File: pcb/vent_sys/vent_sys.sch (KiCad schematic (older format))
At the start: 19 parts, among them J1 Conn_01x02_Female, J2 Conn_01x02_Female, Q1 BT138-600, U1 PC817, U2 stm32f103c8t6-module-china, U3 MOC3021M, U4 RA-02

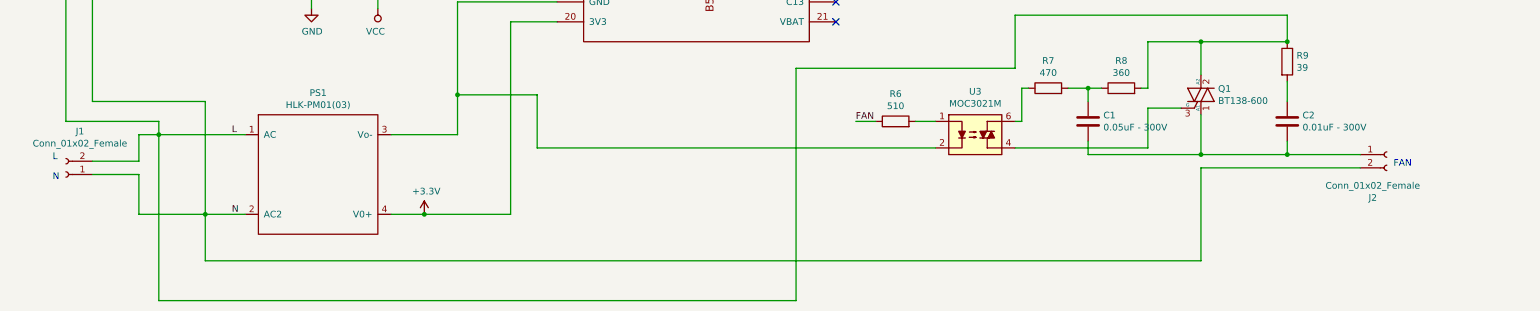
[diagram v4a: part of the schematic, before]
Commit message: add net list and foot prints
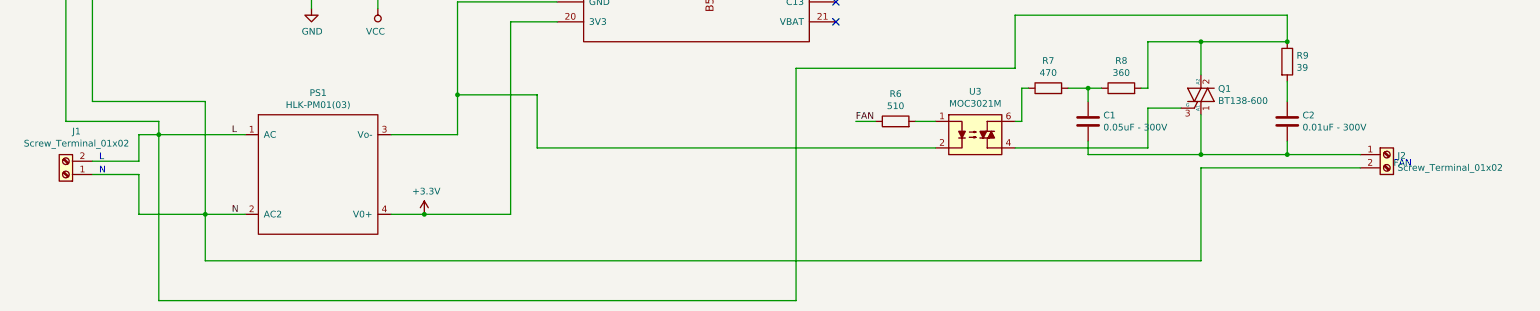
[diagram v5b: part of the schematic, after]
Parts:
- removed J1, J2: Conn_01x02_Female, symbol Connector:Conn_01x02_Female
- added J1, J2: Screw_Terminal_01x02, Connector_Phoenix_MC_HighVoltage:PhoenixContact_MCV_1,5_2-G-5.08_1x02_P5.08mm_Vertical, symbol Connector:Screw_Terminal_01x02
- C1: footprint (none) -> Capacitor_THT:C_Rect_L10.0mm_W2.5mm_P7.50mm_MKS4
- C2: footprint (none) -> Capacitor_THT:C_Rect_L9.0mm_W9.8mm_P7.50mm_MKT
- R6: footprint (none) -> Resistor_SMD:R_0805_2012Metric_Pad1.15x1.40mm_HandSolder
- R7, R8, R9: footprint (none) -> Resistor_THT:R_Axial_DIN0207_L6.3mm_D2.5mm_P10.16mm_Horizontal
- U2: footprint (none) -> Module:Maple_Mini
- U3: footprint (none) -> Package_DIP:DIP-6_W10.16mm
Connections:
- net L: now also J1.2 (Pin_2)
- net N: now also J1.1 (Pin_1), J2.2 (Pin_2)
- net at C1.2, C2.2, Q1.1 (A1): now also J2.1 (Pin_1)
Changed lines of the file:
@@
 F 0 "U2" H 5700 4837 60  0000 C CNN
 F 1 "stm32f103c8t6-module-china" H 5700 4731 60  0000 C CNN
-F 2 "" H 5700 1400 60  0001 C CNN
+F 2 "Module:Maple_Mini" H 5700 1400 60  0001 C CNN
 F 3 "" H 5300 3350 60  0000 C CNN
 	1    5700 3100
@@
 $EndComp
 $Comp
-L power:+3.3V #PWR04
+L power:+3.3V #PWR05
 U 1 1 5C5AFAD4
 P 3650 6000
-F 0 "#PWR04" H 3650 5850 50  0001 C CNN
+F 0 "#PWR05" H 3650 5850 50  0001 C CNN
 F 1 "+3.3V" H 3665 6173 50  0000 C CNN
 F 2 "" H 3650 6000 50  0001 C CNN
@@
 Wire Wire Line
 	3400 6000 3650 6000
-$Comp
-L Connector:Conn_01x02_Female J1
-U 1 1 5C5B0053
-P 950 5700
-F 0 "J1" H 844 5375 50  0000 C CNN
-F 1 "Conn_01x02_Female" H 844 5466 50  0000 C CNN
-F 2 "" H 950 5700 50  0001 C CNN
-F 3 "~" H 950 5700 50  0001 C CNN
-	1    950  5700
-	-1   0    0    1
-$EndComp
 $Comp
 L Device:R R3
@@
 Connection ~ 3650 6000
 $Comp
-L power:GND #PWR05
+L power:GND #PWR06
 U 1 1 5C5B0D6D
 P 7250 1500
-F 0 "#PWR05" H 7250 1250 50  0001 C CNN
+F 0 "#PWR06" H 7250 1250 50  0001 C CNN
 F 1 "GND" H 7255 1327 50  0000 C CNN
 F 2 "" H 7250 1500 50  0001 C CNN
@@
 	2800 2650 2800 2500
 $Comp
-L power:+3.3V #PWR06
+L power:+3.3V #PWR07
 U 1 1 5C5B5B03
 P 7500 1800
-F 0 "#PWR06" H 7500 1650 50  0001 C CNN
+F 0 "#PWR07" H 7500 1650 50  0001 C CNN
 F 1 "+3.3V" H 7515 1973 50  0000 C CNN
 F 2 "" H 7500 1800 50  0001 C CNN
@@
 	1650 5400 2300 5400
 $Comp
-L power:GND #PWR07
+L power:GND #PWR08
 U 1 1 5C5D7125
 P 7750 850
-F 0 "#PWR07" H 7750 600 50  0001 C CNN
+F 0 "#PWR08" H 7750 600 50  0001 C CNN
 F 1 "GND" H 7755 677 50  0000 C CNN
 F 2 "" H 7750 850 50  0001 C CNN
@@
 Connection ~ 8400 900
 $Comp
-L power:+3.3V #PWR08
+L power:+3.3V #PWR09
 U 1 1 5C5DA605
 P 8000 1100
-F 0 "#PWR08" H 8000 950 50  0001 C CNN
+F 0 "#PWR09" H 8000 950 50  0001 C CNN
 F 1 "+3.3V" H 8015 1273 50  0000 C CNN
 F 2 "" H 8000 1100 50  0001 C CNN
@@
 Wire Wire Line
 	8000 1100 8500 1100
-Text Notes 850  5600 0    50   ~ 0
+Text Notes 1200 5600 0    50   ~ 0
 L
-Text Notes 850  5750 0    50   ~ 0
+Text Notes 1200 5700 0    50   ~ 0
 N
 Wire Wire Line
@@
 	8700 2900 8700 2200
 $Comp
-L power:PWR_FLAG #FLG02
+L power:PWR_FLAG #FLG01
 U 1 1 5C8AB50F
 P 2800 4350
-F 0 "#FLG02" H 2800 4425 50  0001 C CNN
+F 0 "#FLG01" H 2800 4425 50  0001 C CNN
 F 1 "PWR_FLAG" H 2800 4524 50  0000 C CNN
 F 2 "" H 2800 4350 50  0001 C CNN
@@
 $EndComp
 $Comp
-L power:PWR_FLAG #FLG01
+L power:PWR_FLAG #FLG02
 U 1 1 5C8AB681
 P 3300 4350
-F 0 "#FLG01" H 3300 4425 50  0001 C CNN
+F 0 "#FLG02" H 3300 4425 50  0001 C CNN
 F 1 "PWR_FLAG" H 3300 4524 50  0000 C CNN
 F 2 "" H 3300 4350 50  0001 C CNN
@@
 SCK
 $Comp
-L power:GND #PWR09
+L power:GND #PWR010
 U 1 1 5C8D193A
 P 9600 1700
-F 0 "#PWR09" H 9600 1450 50  0001 C CNN
+F 0 "#PWR010" H 9600 1450 50  0001 C CNN
 F 1 "GND" H 9605 1527 50  0000 C CNN
 F 2 "" H 9600 1700 50  0001 C CNN
@@
 	9600 1600 9600 1700
 $Comp
-L power:GND #PWR010
+L power:GND #PWR011
 U 1 1 5C8D5889
 P 9750 700
-F 0 "#PWR010" H 9750 450 50  0001 C CNN
+F 0 "#PWR011" H 9750 450 50  0001 C CNN
 F 1 "GND" H 9755 527 50  0000 C CNN
 F 2 "" H 9750 700 50  0001 C CNN
@@
 F 0 "C2" H 10265 5346 50  0000 L CNN
 F 1 "0.01uF - 300V" H 10265 5255 50  0000 L CNN
-F 2 "" H 10188 5150 50  0001 C CNN
+F 2 "Capacitor_THT:C_Rect_L9.0mm_W9.8mm_P7.50mm_MKT" H 10188 5150 50  0001 C CNN
 F 3 "~" H 10150 5300 50  0001 C CNN
 	1    10150 5300
@@
 F 0 "R9" H 10220 4896 50  0000 L CNN
 F 1 "39" H 10220 4805 50  0000 L CNN
-F 2 "" V 10080 4850 50  0001 C CNN
+F 2 "Resistor_THT:R_Axial_DIN0207_L6.3mm_D2.5mm_P10.16mm_Horizontal" V 10080 4850 50  0001 C CNN
 F 3 "~" H 10150 4850 50  0001 C CNN
 	1    10150 4850
@@
 F 0 "R7" V 8557 5050 50  0000 C CNN
 F 1 "470" V 8466 5050 50  0000 C CNN
-F 2 "" V 8280 5050 50  0001 C CNN
+F 2 "Resistor_THT:R_Axial_DIN0207_L6.3mm_D2.5mm_P10.16mm_Horizontal" V 8280 5050 50  0001 C CNN
 F 3 "~" H 8350 5050 50  0001 C CNN
 	1    8350 5050
@@
 F 0 "R8" V 9107 5050 50  0000 C CNN
 F 1 "360" V 9016 5050 50  0000 C CNN
-F 2 "" V 8830 5050 50  0001 C CNN
+F 2 "Resistor_THT:R_Axial_DIN0207_L6.3mm_D2.5mm_P10.16mm_Horizontal" V 8830 5050 50  0001 C CNN
 F 3 "~" H 8900 5050 50  0001 C CNN
 	1    8900 5050
@@
 Text Notes 10950 5650 0    50   ~ 0
 FAN
-$Comp
-L Connector:Conn_01x02_Female J2
-U 1 1 5C5DC3CB
-P 10900 5550
-F 0 "J2" H 10794 5225 50  0000 C CNN
-F 1 "Conn_01x02_Female" H 10794 5316 50  0000 C CNN
-F 2 "" H 10900 5550 50  0001 C CNN
-F 3 "~" H 10900 5550 50  0001 C CNN
-	1    10900 5550
-	1    0    0    -1
-$EndComp
 $Comp
 L Device:C C1
@@
 F 0 "C1" H 8765 5346 50  0000 L CNN
 F 1 "0.05uF - 300V" H 8765 5255 50  0000 L CNN
-F 2 "" H 8688 5150 50  0001 C CNN
+F 2 "Capacitor_THT:C_Rect_L10.0mm_W2.5mm_P7.50mm_MKS4" H 8688 5150 50  0001 C CNN
 F 3 "~" H 8650 5300 50  0001 C CNN
 	1    8650 5300
@@
 F 0 "U3" H 7800 5725 50  0000 C CNN
 F 1 "MOC3021M" H 7800 5634 50  0000 C CNN
-F 2 "" H 7600 5200 50  0001 L CIN
+F 2 "Package_DIP:DIP-6_W10.16mm" H 7600 5200 50  0001 L CIN
 F 3 "http://www.fairchildsemi.com/ds/MO/MOC3020M.pdf" H 7775 5400 50  0001 L CNN
 	1    7800 5400
@@
 F 0 "R6" V 7407 5300 50  0000 C CNN
 F 1 "510" V 7316 5300 50  0000 C CNN
-F 2 "" V 7130 5300 50  0001 C CNN
+F 2 "Resistor_SMD:R_0805_2012Metric_Pad1.15x1.40mm_HandSolder" V 7130 5300 50  0001 C CNN
 F 3 "~" H 7200 5300 50  0001 C CNN
 	1    7200 5300
@@
 	3650 6000 4300 6000
 $Comp
-L power:GND #PWR0101
+L power:GND #PWR03
 U 1 1 5C9B68E2
 P 2800 4450
-F 0 "#PWR0101" H 2800 4200 50  0001 C CNN
+F 0 "#PWR03" H 2800 4200 50  0001 C CNN
 F 1 "GND" H 2805 4277 50  0000 C CNN
 F 2 "" H 2800 4450 50  0001 C CNN
@@
 	2800 4350 2800 4450
 $Comp
-L power:VCC #PWR0102
+L power:VCC #PWR04
 U 1 1 5C9BB0DE
 P 3300 4450
-F 0 "#PWR0102" H 3300 4300 50  0001 C CNN
+F 0 "#PWR04" H 3300 4300 50  0001 C CNN
 F 1 "VCC" H 3318 4623 50  0000 C CNN
 F 2 "" H 3300 4450 50  0001 C CNN
@@
 Wire Wire Line
 	2800 3050 3500 3050
+$Comp
+L Connector:Screw_Terminal_01x02 J2
+U 1 1 5C92A326
+P 10900 5550
+F 0 "J2" H 10980 5542 50  0000 L CNN
+F 1 "Screw_Terminal_01x02" H 10980 5451 50  0000 L CNN
+F 2 "Connector_Phoenix_MC_HighVoltage:PhoenixContact_MCV_1,5_2-G-5.08_1x02_P5.08mm_Vertical" H 10900 5550 50  0001 C CNN
+F 3 "~" H 10900 5550 50  0001 C CNN
+	1    10900 5550
+	1    0    0    -1
+$EndComp
+$Comp
+L Connector:Screw_Terminal_01x02 J1
+U 1 1 5C92A382
+P 950 5700
+F 0 "J1" H 870 5375 50  0000 C CNN
+F 1 "Screw_Terminal_01x02" H 870 5466 50  0000 C CNN
+F 2 "Connector_Phoenix_MC_HighVoltage:PhoenixContact_MCV_1,5_2-G-5.08_1x02_P5.08mm_Vertical" H 950 5700 50  0001 C CNN
+F 3 "~" H 950 5700 50  0001 C CNN
+	1    950  5700
+	-1   0    0    1
+$EndComp
 Wire Bus Line
 	10800 750  10800 2100

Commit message: pcb trace
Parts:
- added R10, R11: 5K, Resistor_SMD:R_1206_3216Metric, symbol Device:R
- PS1: footprint HLK-PM01:HLK-PM01 -> Converter_ACDC:HLK-PM01
- U2: symbol stm32f103c8t6-module-china:stm32f103c8t6-module-china -> vent_sys-rescue:stm32f103c8t6-module-china-stm32f103c8t6-module-china
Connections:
- net GND: now also PS1.3 (Vo-), U2.19 (GND), U3.2; no longer U2.39 (GND), U2.40 (GND), U4.1 (gnd), U4.16 (gnd), U4.2 (gnd), U4.9 (gnd)
- net MISO: now also R11.1; no longer U4.13 (miso)
- net MOSI: now also R10.2; no longer U4.14 (mosi)
- net VCC: now also PS1.4 (V0+), U2.20 (3V3)
- net at U2.24 (C15/OSC32_OUT): now also R6.1
- net +3V3: no longer names the net of R5.1, U2.38 (3V3), U4.3 (3v3)
- net +3V3: no longer PS1.4 (V0+), U2.20 (3V3)
- net FAN: no longer names the net of U2.35 (B10/SCL2/U3TX)
- net FAN: no longer R6.1
- new net: U2.39 (GND), U2.40 (GND), U4.1 (gnd), U4.16 (gnd), U4.2 (gnd), U4.9 (gnd)
- new net: R11.2, U4.13 (miso)
- new net: R10.1, U4.14 (mosi)
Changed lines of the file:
@@
 $EndDescr
 $Comp
-L stm32f103c8t6-module-china:stm32f103c8t6-module-china U2
+L vent_sys-rescue:stm32f103c8t6-module-china-stm32f103c8t6-module-china U2
 U 1 1 5C5569F8
 P 5700 3100
@@
 F 0 "PS1" H 2850 6315 50  0000 C CNN
 F 1 "HLK-PM01(03)" H 2850 6224 50  0000 C CNN
-F 2 "HLK-PM01:HLK-PM01" H 2850 5700 50  0001 C CNN
+F 2 "Converter_ACDC:HLK-PM01" H 2850 5700 50  0001 C CNN
 F 3 "" H 2850 5700 50  0001 C CNN
 	1    2850 5700
@@
 	1    0    0    -1
 $EndComp
-$Comp
-L power:+3.3V #PWR05
-U 1 1 5C5AFAD4
-P 3650 6000
-F 0 "#PWR05" H 3650 5850 50  0001 C CNN
-F 1 "+3.3V" H 3665 6173 50  0000 C CNN
-F 2 "" H 3650 6000 50  0001 C CNN
-F 3 "" H 3650 6000 50  0001 C CNN
-	1    3650 6000
-	1    0    0    -1
-$EndComp
-Wire Wire Line
-	3400 6000 3650 6000
 $Comp
 L Device:R R3
@@
 Wire Wire Line
 	4300 4550 4300 6000
-Connection ~ 3650 6000
-$Comp
-L power:GND #PWR06
-U 1 1 5C5B0D6D
-P 7250 1500
-F 0 "#PWR06" H 7250 1250 50  0001 C CNN
-F 1 "GND" H 7255 1327 50  0000 C CNN
-F 2 "" H 7250 1500 50  0001 C CNN
-F 3 "" H 7250 1500 50  0001 C CNN
-	1    7250 1500
-	1    0    0    -1
-$EndComp
-Wire Wire Line
-	6750 1700 6900 1700
-Wire Wire Line
-	6900 1700 6900 1400
-Wire Wire Line
-	6900 1400 7250 1400
-Wire Wire Line
-	7250 1400 7250 1500
-Wire Wire Line
-	6750 1850 6900 1850
-Wire Wire Line
-	6900 1850 6900 1700
-Connection ~ 6900 1700
-Wire Wire Line
-	4650 4400 3900 4400
-Wire Wire Line
-	3900 4400 3900 5100
 Wire Wire Line
 	1800 2900 1800 3050
@@
 Wire Wire Line
 	2800 3050 2800 2950
-$Comp
-L power:+3.3V #PWR02
-U 1 1 5C5B4551
-P 2800 2500
-F 0 "#PWR02" H 2800 2350 50  0001 C CNN
-F 1 "+3.3V" H 2815 2673 50  0000 C CNN
-F 2 "" H 2800 2500 50  0001 C CNN
-F 3 "" H 2800 2500 50  0001 C CNN
-	1    2800 2500
-	1    0    0    -1
-$EndComp
-Wire Wire Line
-	2800 2650 2800 2500
-$Comp
-L power:+3.3V #PWR07
-U 1 1 5C5B5B03
-P 7500 1800
-F 0 "#PWR07" H 7500 1650 50  0001 C CNN
-F 1 "+3.3V" H 7515 1973 50  0000 C CNN
-F 2 "" H 7500 1800 50  0001 C CNN
-F 3 "" H 7500 1800 50  0001 C CNN
-	1    7500 1800
-	1    0    0    -1
-$EndComp
-Wire Wire Line
-	6750 2000 7500 2000
-Wire Wire Line
-	7500 2000 7500 1800
 Wire Wire Line
 	1200 3350 1150 3350
@@
 Wire Wire Line
 	1650 5400 2300 5400
-$Comp
-L power:GND #PWR08
-U 1 1 5C5D7125
-P 7750 850
-F 0 "#PWR08" H 7750 600 50  0001 C CNN
-F 1 "GND" H 7755 677 50  0000 C CNN
-F 2 "" H 7750 850 50  0001 C CNN
-F 3 "" H 7750 850 50  0001 C CNN
-	1    7750 850
-	1    0    0    -1
-$EndComp
 Wire Wire Line
 	8500 900  8400 900
 Wire Wire Line
-	8400 900  8400 750
-Wire Wire Line
-	8400 750  7750 750
-Wire Wire Line
-	7750 750  7750 850
-Wire Wire Line
 	8500 1000 8400 1000
 Wire Wire Line
 	8400 1000 8400 900
-Connection ~ 8400 900
-$Comp
-L power:+3.3V #PWR09
-U 1 1 5C5DA605
-P 8000 1100
-F 0 "#PWR09" H 8000 950 50  0001 C CNN
-F 1 "+3.3V" H 8015 1273 50  0000 C CNN
-F 2 "" H 8000 1100 50  0001 C CNN
-F 3 "" H 8000 1100 50  0001 C CNN
-	1    8000 1100
-	1    0    0    -1
-$EndComp
-Wire Wire Line
-	8000 1100 8500 1100
 Text Notes 1200 5600 0    50   ~ 0
 L
@@
 Wire Wire Line
 	8700 2900 8700 2200
-$Comp
-L power:PWR_FLAG #FLG01
-U 1 1 5C8AB50F
-P 2800 4350
-F 0 "#FLG01" H 2800 4425 50  0001 C CNN
-F 1 "PWR_FLAG" H 2800 4524 50  0000 C CNN
-F 2 "" H 2800 4350 50  0001 C CNN
-F 3 "~" H 2800 4350 50  0001 C CNN
-	1    2800 4350
-	1    0    0    -1
-$EndComp
-$Comp
-L power:PWR_FLAG #FLG02
-U 1 1 5C8AB681
-P 3300 4350
-F 0 "#FLG02" H 3300 4425 50  0001 C CNN
-F 1 "PWR_FLAG" H 3300 4524 50  0000 C CNN
-F 2 "" H 3300 4350 50  0001 C CNN
-F 3 "~" H 3300 4350 50  0001 C CNN
-	1    3300 4350
-	1    0    0    -1
-$EndComp
 Text Label 7300 2900 0    50   ~ 0
 MOSI
@@
 	9500 1000 10700 1000
 Wire Wire Line
-	9500 1100 10700 1100
-Wire Wire Line
-	9500 1200 10700 1200
-Wire Wire Line
 	9500 1300 10700 1300
 Entry Wire Line
@@
 Text Label 9850 1000 0    50   ~ 0
 NSS
-Text Label 9850 1100 0    50   ~ 0
+Text Label 10500 1100 0    50   ~ 0
 MOSI
-Text Label 9850 1200 0    50   ~ 0
+Text Label 10500 1200 0    50   ~ 0
 MISO
 Text Label 9850 1300 0    50   ~ 0
 SCK
-$Comp
-L power:GND #PWR010
-U 1 1 5C8D193A
-P 9600 1700
-F 0 "#PWR010" H 9600 1450 50  0001 C CNN
-F 1 "GND" H 9605 1527 50  0000 C CNN
-F 2 "" H 9600 1700 50  0001 C CNN
-F 3 "" H 9600 1700 50  0001 C CNN
-	1    9600 1700
-	1    0    0    -1
-$EndComp
-Wire Wire Line
-	9500 1600 9600 1600
-Wire Wire Line
-	9600 1600 9600 1700
-$Comp
-L power:GND #PWR011
-U 1 1 5C8D5889
-P 9750 700
-F 0 "#PWR011" H 9750 450 50  0001 C CNN
-F 1 "GND" H 9755 527 50  0000 C CNN
-F 2 "" H 9750 700 50  0001 C CNN
-F 3 "" H 9750 700 50  0001 C CNN
-	1    9750 700
-	1    0    0    -1
-$EndComp
-Wire Wire Line
-	9500 900  9500 600
-Wire Wire Line
-	9500 600  9750 600
-Wire Wire Line
-	9750 600  9750 700
 Wire Wire Line
 	6750 3500 9100 3500
@@
 Wire Wire Line
 	7350 5300 7500 5300
-Text Label 6900 5300 0    50   ~ 0
-FAN
-Text Label 7100 2450 0    50   ~ 0
-FAN
-Wire Wire Line
-	7050 5300 6900 5300
-Wire Wire Line
-	6750 2450 7100 2450
-Wire Wire Line
-	7500 5500 4500 5500
-Wire Wire Line
-	4500 5500 4500 5100
-Wire Wire Line
-	4500 5100 3900 5100
-Connection ~ 3900 5100
-Wire Wire Line
-	3900 5100 3900 5400
 Connection ~ 2800 3050
 Entry Wire Line
@@
 NoConn ~ 6750 4400
 NoConn ~ 6750 4250
-NoConn ~ 6750 4100
 NoConn ~ 6750 3950
 NoConn ~ 4650 1850
@@
 NoConn ~ 6750 2150
 NoConn ~ 10900 3300
-Wire Wire Line
-	3650 6000 4300 6000
-$Comp
-L power:GND #PWR03
-U 1 1 5C9B68E2
-P 2800 4450
-F 0 "#PWR03" H 2800 4200 50  0001 C CNN
-F 1 "GND" H 2805 4277 50  0000 C CNN
-F 2 "" H 2800 4450 50  0001 C CNN
-F 3 "" H 2800 4450 50  0001 C CNN
-	1    2800 4450
-	1    0    0    -1
-$EndComp
-Wire Wire Line
-	2800 4350 2800 4450
-$Comp
-L power:VCC #PWR04
-U 1 1 5C9BB0DE
-P 3300 4450
-F 0 "#PWR04" H 3300 4300 50  0001 C CNN
-F 1 "VCC" H 3318 4623 50  0000 C CNN
-F 2 "" H 3300 4450 50  0001 C CNN
-F 3 "" H 3300 4450 50  0001 C CNN
-	1    3300 4450
-	-1   0    0    1
-$EndComp
-Wire Wire Line
-	3300 4350 3300 4450
 NoConn ~ 9500 1400
 NoConn ~ 9500 1500
 NoConn ~ 8500 1500
 NoConn ~ 8500 1600
-Wire Wire Line
-	3400 5400 3900 5400
 Wire Wire Line
 	4650 1700 3500 1700
@@
 	-1   0    0    1
 $EndComp
+$Comp
+L power:GND #PWR0103
+U 1 1 5C986FC8
+P 7150 5600
+F 0 "#PWR0103" H 7150 5350 50  0001 C CNN
+F 1 "GND" H 7155 5427 50  0000 C CNN
+F 2 "" H 7150 5600 50  0001 C CNN
+F 3 "" H 7150 5600 50  0001 C CNN
+	1    7150 5600
+	1    0    0    -1
+$EndComp
+Wire Wire Line
+	7150 5500 7150 5600
+Wire Wire Line
+	3400 6000 3950 6000
+Wire Wire Line
+	3400 5400 3700 5400
+$Comp
+L power:GND #PWR0101
+U 1 1 5C9AEA36
+P 3700 5500
+F 0 "#PWR0101" H 3700 5250 50  0001 C CNN
+F 1 "GND" H 3705 5327 50  0000 C CNN
+F 2 "" H 3700 5500 50  0001 C CNN
+F 3 "" H 3700 5500 50  0001 C CNN
+	1    3700 5500
+	1    0    0    -1
+$EndComp
+Wire Wire Line
+	3700 5500 3700 5400
+Wire Wire Line
+	7150 5500 7500 5500
+Wire Wire Line
+	9500 900  9500 600
+Connection ~ 8400 900
+Wire Wire Line
+	8400 600  8400 900
+Wire Wire Line
+	9500 600  8400 600
+Wire Wire Line
+	6900 1850 6900 1700
+Wire Wire Line
+	4650 4400 4000 4400
+Wire Wire Line
+	6750 1850 6900 1850
+Wire Wire Line
+	6750 1700 6900 1700
+Connection ~ 6900 1700
+$Comp
+L power:VCC #PWR0107
+U 1 1 5C98C187
+P 3950 5900
+F 0 "#PWR0107" H 3950 5750 50  0001 C CNN
+F 1 "VCC" H 3967 6073 50  0000 C CNN
+F 2 "" H 3950 5900 50  0001 C CNN
+F 3 "" H 3950 5900 50  0001 C CNN
+	1    3950 5900
+	1    0    0    -1
+$EndComp
+Wire Wire Line
+	3950 5900 3950 6000
+Connection ~ 3950 6000
+Wire Wire Line
+	3950 6000 4300 6000
+Wire Wire Line
+	7700 1100 8500 1100
+Wire Wire Line
+	4000 4400 4000 5400
+Wire Wire Line
+	4000 5400 3700 5400
+Connection ~ 3700 5400
+Wire Wire Line
+	6900 600  8400 600
+Wire Wire Line
+	6900 600  6900 1700
+Connection ~ 8400 600
+Wire Wire Line
+	9500 1600 9800 1600
+Wire Wire Line
+	9800 1600 9800 600
+Wire Wire Line
+	9800 600  9500 600
+Connection ~ 9500 600
+Wire Wire Line
+	7700 2000 7700 1100
+Wire Wire Line
+	6750 2000 7700 2000
+Wire Wire Line
+	2800 2650 2800 1100
+Wire Wire Line
+	2800 1100 7700 1100
+Connection ~ 7700 1100
+NoConn ~ 6750 2450
+Wire Wire Line
+	6750 4100 6900 4100
+Wire Wire Line
+	6900 4100 6900 5300
+Wire Wire Line
+	6900 5300 7050 5300
+$Comp
+L Device:R R10
+U 1 1 5C980FE3
+P 10250 1100
+F 0 "R10" H 10320 1146 50  0000 L CNN
+F 1 "5K" H 10320 1055 50  0000 L CNN
+F 2 "Resistor_SMD:R_1206_3216Metric" V 10180 1100 50  0001 C CNN
+F 3 "~" H 10250 1100 50  0001 C CNN
+	1    10250 1100
+	0    -1   -1   0
+$EndComp
+$Comp
+L Device:R R11
+U 1 1 5C9A026E
+P 10250 1200
+F 0 "R11" H 10320 1246 50  0000 L CNN
+F 1 "5K" H 10320 1155 50  0000 L CNN
+F 2 "Resistor_SMD:R_1206_3216Metric" V 10180 1200 50  0001 C CNN
+F 3 "~" H 10250 1200 50  0001 C CNN
+	1    10250 1200
+	0    1    1    0
+$EndComp
+Wire Wire Line
+	10400 1100 10700 1100
+Wire Wire Line
+	10700 1200 10400 1200
+Wire Wire Line
+	9500 1100 10100 1100
+Wire Wire Line
+	10100 1200 9500 1200
 Wire Bus Line
 	10800 750  10800 2100

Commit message: PCB trace completed
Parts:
- removed R10, R11: 5K, Resistor_SMD:R_1206_3216Metric, symbol Device:R
- C2: footprint Capacitor_THT:C_Rect_L9.0mm_W9.8mm_P7.50mm_MKT -> Capacitor_THT:C_Rect_L9.0mm_W3.2mm_P7.50mm_MKT
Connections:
- net MISO: now also U4.13 (miso)
- net MOSI: now also U4.14 (mosi)
- net VCC: now also R5.1, U2.38 (3V3), U4.3 (3v3)
- net at U2.39 (GND), U2.40 (GND), U4.16 (gnd): no longer U4.1 (gnd), U4.2 (gnd), U4.9 (gnd)
- no-connect marks 31 -> 34
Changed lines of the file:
@@
 Wire Wire Line
 	1650 5400 2300 5400
-Wire Wire Line
-	8500 900  8400 900
-Wire Wire Line
-	8500 1000 8400 1000
-Wire Wire Line
-	8400 1000 8400 900
 Text Notes 1200 5600 0    50   ~ 0
 L
@@
 Text Label 9850 1000 0    50   ~ 0
 NSS
-Text Label 10500 1100 0    50   ~ 0
+Text Label 9850 1100 0    50   ~ 0
 MOSI
-Text Label 10500 1200 0    50   ~ 0
+Text Label 9850 1200 0    50   ~ 0
 MISO
 Text Label 9850 1300 0    50   ~ 0
@@
 F 0 "C2" H 10265 5346 50  0000 L CNN
 F 1 "0.01uF - 300V" H 10265 5255 50  0000 L CNN
-F 2 "Capacitor_THT:C_Rect_L9.0mm_W9.8mm_P7.50mm_MKT" H 10188 5150 50  0001 C CNN
+F 2 "Capacitor_THT:C_Rect_L9.0mm_W3.2mm_P7.50mm_MKT" H 10188 5150 50  0001 C CNN
 F 3 "~" H 10150 5300 50  0001 C CNN
 	1    10150 5300
@@
 Wire Wire Line
 	9500 900  9500 600
-Connection ~ 8400 900
-Wire Wire Line
-	8400 600  8400 900
-Wire Wire Line
-	9500 600  8400 600
 Wire Wire Line
 	6900 1850 6900 1700
@@
 Connection ~ 3700 5400
 Wire Wire Line
-	6900 600  8400 600
-Wire Wire Line
 	6900 600  6900 1700
-Connection ~ 8400 600
-Wire Wire Line
-	9500 1600 9800 1600
-Wire Wire Line
-	9800 1600 9800 600
-Wire Wire Line
-	9800 600  9500 600
-Connection ~ 9500 600
 Wire Wire Line
 	7700 2000 7700 1100
@@
 	6900 5300 7050 5300
 $Comp
-L Device:R R10
-U 1 1 5C980FE3
-P 10250 1100
-F 0 "R10" H 10320 1146 50  0000 L CNN
-F 1 "5K" H 10320 1055 50  0000 L CNN
-F 2 "Resistor_SMD:R_1206_3216Metric" V 10180 1100 50  0001 C CNN
-F 3 "~" H 10250 1100 50  0001 C CNN
-	1    10250 1100
-	0    -1   -1   0
-$EndComp
-$Comp
-L Device:R R11
-U 1 1 5C9A026E
-P 10250 1200
-F 0 "R11" H 10320 1246 50  0000 L CNN
-F 1 "5K" H 10320 1155 50  0000 L CNN
-F 2 "Resistor_SMD:R_1206_3216Metric" V 10180 1200 50  0001 C CNN
-F 3 "~" H 10250 1200 50  0001 C CNN
-	1    10250 1200
-	0    1    1    0
-$EndComp
-Wire Wire Line
-	10400 1100 10700 1100
-Wire Wire Line
-	10700 1200 10400 1200
-Wire Wire Line
-	9500 1100 10100 1100
-Wire Wire Line
-	10100 1200 9500 1200
+L power:VCC #PWR0102
+U 1 1 5C9B7B47
+P 7700 950
+F 0 "#PWR0102" H 7700 800 50  0001 C CNN
+F 1 "VCC" H 7717 1123 50  0000 C CNN
+F 2 "" H 7700 950 50  0001 C CNN
+F 3 "" H 7700 950 50  0001 C CNN
+	1    7700 950
+	1    0    0    -1
+$EndComp
+Wire Wire Line
+	7700 950  7700 1100
+Wire Wire Line
+	9500 1100 10700 1100
+Wire Wire Line
+	9500 1200 10700 1200
+Wire Wire Line
+	6900 600  9500 600
+NoConn ~ 9500 1600
+NoConn ~ 8500 1000
+NoConn ~ 8500 900
 Wire Bus Line
 	10800 750  10800 2100

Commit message: final
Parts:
- U3: footprint Package_DIP:DIP-6_W10.16mm -> Package_DIP:DIP-6_W7.62mm_Socket_LongPads
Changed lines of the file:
@@
 F 0 "U3" H 7800 5725 50  0000 C CNN
 F 1 "MOC3021M" H 7800 5634 50  0000 C CNN
-F 2 "Package_DIP:DIP-6_W10.16mm" H 7600 5200 50  0001 L CIN
+F 2 "Package_DIP:DIP-6_W7.62mm_Socket_LongPads" H 7600 5200 50  0001 L CIN
 F 3 "http://www.fairchildsemi.com/ds/MO/MOC3020M.pdf" H 7775 5400 50  0001 L CNN
 	1    7800 5400
